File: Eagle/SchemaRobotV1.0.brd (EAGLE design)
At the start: 106 x 60 mm, 24 parts, among them J1 Connector US1, J2 Connector US 2, J3 Connector US 2, J4 Connector H-Brug, J5 Connector IR voeding, J6 Connector IR signalen, J7 Connector batterij 12v, J9 Connector HC-05

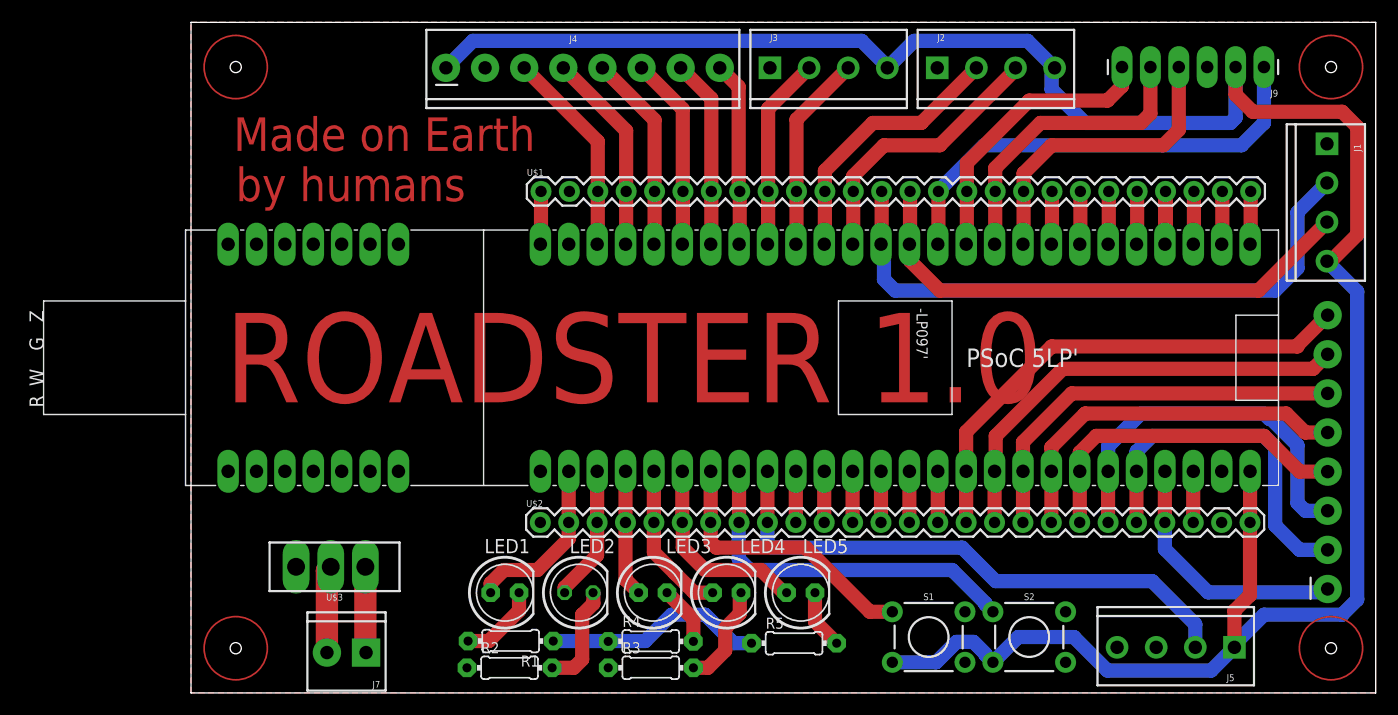
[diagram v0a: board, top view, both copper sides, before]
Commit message: eagle
meer padjes van top naar bottom
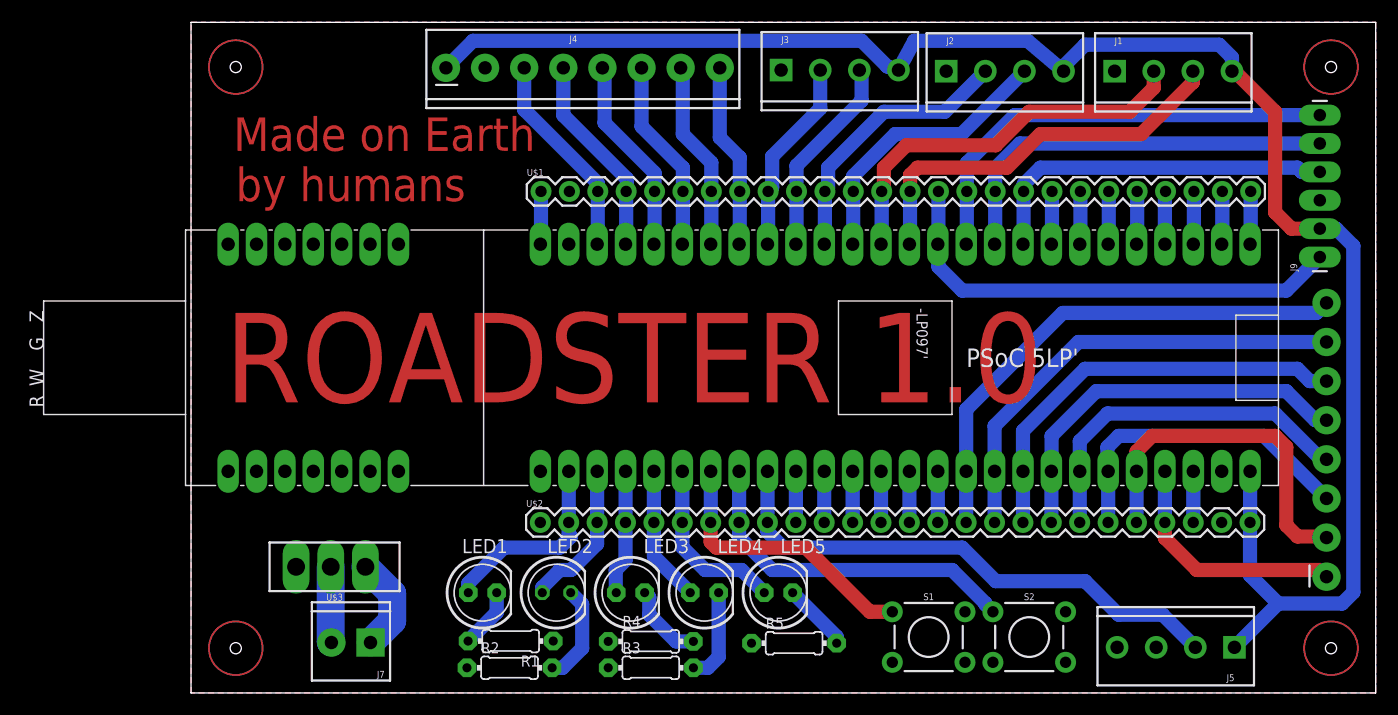
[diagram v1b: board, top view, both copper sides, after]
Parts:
- moved J1 20.1 mm to (82.6, 55.6), turned to 0 degrees
- moved J9 17.7 mm to (101.0, 39.0), turned to 90 degrees
- moved LED1 2.00 mm to (26.1, 8.97)
- moved LED2 2.00 mm to (32.7, 8.97)
- moved LED3 2.00 mm to (39.3, 8.97)
- moved LED4 2.00 mm to (45.9, 8.97)
- moved LED5 2.00 mm to (52.6, 8.97)
- moved J6 1.10 mm to (101.6, 10.4)
- moved J3 1.02 mm to (52.8, 55.7)
- moved J7 0.98 mm to (16.1, 4.51)
- moved J2 0.85 mm to (67.6, 55.6)
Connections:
- net GND: now also S1.3, S2.3
- net VCC: no longer S1.3, S2.3
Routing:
- net VCC: track 206.8 -> 157.0 mm
- net GND: track 19.8 -> 0.00 mm
- net P12.2: track 55.0 -> 35.5 mm
- net P12.5: track 25.7 -> 40.6 mm
- net P12.3: track 47.2 -> 35.9 mm
- net P12.6: track 26.9 -> 36.8 mm
- net P0.5: track 34.3 -> 29.1 mm
- net P12.7: track 27.5 -> 32.7 mm
- net P2.3: track 9.70 -> 4.75 mm
- net P3.0: track 15.5 -> 17.7 mm
- net P3.4: track 17.8 -> 15.8 mm
- net N$2: track 7.30 -> 5.39 mm
- net P0.2: track 36.3 -> 38.1 mm
- net P3.7: track 49.8 -> 48.0 mm
- net P3.3: track 14.0 -> 12.2 mm
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- added copper zone on layer 16, net GND

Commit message: eagle
padjes verbeterd
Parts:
- LED2: device led:LED5MM -> SchemaRobotV1.0:LED_LED5MM
- moved S1 2.00 mm to (64.0, 5.00)
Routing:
- net P3.5: track 25.2 -> 23.2 mm
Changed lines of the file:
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@@
 <setting verticaltext="up"/>
 </settings>
-<grid distance="1" unitdist="mm" unit="mm" style="lines" multiple="1" display="no" altdistance="0.1" altunitdist="mm" altunit="mm"/>
+<grid distance="0.1" unitdist="mm" unit="mm" style="lines" multiple="1" display="no" altdistance="0.1" altunitdist="mm" altunit="mm"/>
 <layers>
-<layer number="1" name="Top" color="4" fill="1" visible="yes" active="yes"/>
+<layer number="1" name="Top" color="4" fill="1" visible="no" active="yes"/>
 <layer number="2" name="Route2" color="1" fill="3" visible="no" active="no"/>
 <layer number="3" name="Route3" color="4" fill="3" visible="no" active="no"/>
@@
 <attribute name="VALUE" x="27.2804" y="6.1666" size="1.27" layer="27" ratio="10"/>
 </element>
-<element name="LED2" library="led" library_urn="urn:adsk.eagle:library:259" package="LED5MM" package3d_urn="urn:adsk.eagle:package:15799/2" value="3.3V" x="32.7" y="8.97" smashed="yes">
+<element name="LED2" library="SchemaRobotV1.0" package="LED_LED5MM" value="3.3V" x="32.7" y="8.97" smashed="yes">
 <attribute name="NAME" x="31.875" y="12.5034" size="1.27" layer="25" ratio="10"/>
 <attribute name="VALUE" x="32.9004" y="6.1666" size="1.27" layer="27" ratio="10"/>
@@
 <element name="U$2" library="SchemaRobotV1.0" package="SPARKFUN-CONNECTORS_1X26" value="SPARKFUN-CONNECTORS_CONN_26" x="31.254" y="15.254"/>
 <element name="J9" library="SchemaRobotV1.0" package="SPARKFUN-CONNECTORS_1X06_LONGPADS" value="Connector HC-05" x="101" y="39" rot="R90"/>
-<element name="S1" library="SchemaRobotV1.0" package="SPARKFUN-SWITCHES_TACTILE_SWITCH_PTH_6.0MM" value="SPARKFUN-SWITCHES_MOMENTARY-SWITCH-SPST-PTH-6.0MM" x="66" y="5">
-<attribute name="PROD_ID" value=" SWCH-08441" x="66" y="5" size="1.778" layer="27" display="off"/>
-<attribute name="SF_SKU" value="COM-00097" x="66" y="5" size="1.778" layer="27" display="off"/>
+<element name="S1" library="SchemaRobotV1.0" package="SPARKFUN-SWITCHES_TACTILE_SWITCH_PTH_6.0MM" value="SPARKFUN-SWITCHES_MOMENTARY-SWITCH-SPST-PTH-6.0MM" x="64" y="5">
+<attribute name="PROD_ID" value=" SWCH-08441" x="64" y="5" size="1.778" layer="27" display="off"/>
+<attribute name="SF_SKU" value="COM-00097" x="64" y="5" size="1.778" layer="27" display="off"/>
 </element>
 <element name="S2" library="SchemaRobotV1.0" package="SPARKFUN-SWITCHES_TACTILE_SWITCH_PTH_6.0MM" value="SPARKFUN-SWITCHES_MOMENTARY-SWITCH-SPST-PTH-6.0MM" x="75" y="5">
@@
 <contactref element="U$2" pad="26"/>
 <contactref element="J9" pad="2"/>
-<wire x1="78.07" y1="55.63" x2="74.851" y2="58.349" width="1.27" layer="16"/>
-<wire x1="64.719" y1="58.349" x2="63.3" y2="55.73" width="1.27" layer="16"/>
-<wire x1="74.851" y1="58.349" x2="64.719" y2="58.349" width="1.27" layer="16"/>
-<wire x1="22.81" y1="55.93" x2="25.229" y2="58.349" width="1.27" layer="16"/>
-<wire x1="25.229" y1="58.349" x2="60" y2="58.349" width="1.27" layer="16"/>
-<wire x1="60" y1="58.349" x2="62.3" y2="56.049" width="1.27" layer="16"/>
-<wire x1="62.3" y1="56.049" x2="63.3" y2="55.73" width="1.27" layer="16"/>
 <wire x1="101" y1="41.54" x2="98.46" y2="41.54" width="1.27" layer="1"/>
 <wire x1="97" y1="43" x2="97" y2="52" width="1.27" layer="1"/>
@@
 <wire x1="93.37" y1="55.63" x2="93.14" y2="55.63" width="1.27" layer="1"/>
 <wire x1="98.46" y1="41.54" x2="97" y2="43" width="1.27" layer="1"/>
-<wire x1="78.07" y1="55.63" x2="78.07" y2="56.07" width="1.27" layer="16"/>
-<wire x1="78.07" y1="56.07" x2="80" y2="58" width="1.27" layer="16"/>
-<wire x1="80" y1="58" x2="92" y2="58" width="1.27" layer="16"/>
-<wire x1="93.14" y1="56.86" x2="93.14" y2="55.63" width="1.27" layer="16"/>
-<wire x1="92" y1="58" x2="93.14" y2="56.86" width="1.27" layer="16"/>
 <wire x1="94.76" y1="19.83" x2="94.76" y2="15.26" width="1.27" layer="16"/>
 <wire x1="94.76" y1="15.26" x2="94.754" y2="15.254" width="1.27" layer="16"/>
@@
 <wire x1="94.754" y1="15.254" x2="94.754" y2="10.526" width="1.27" layer="16"/>
 <wire x1="94.754" y1="10.526" x2="97.28" y2="8" width="1.27" layer="16"/>
+<wire x1="25.229" y1="58.349" x2="22.81" y2="55.93" width="1.27" layer="16"/>
+<wire x1="63.3" y1="55.73" x2="60.681" y2="58.349" width="1.27" layer="16"/>
+<wire x1="60.681" y1="58.349" x2="25.229" y2="58.349" width="1.27" layer="16"/>
+<wire x1="63.3" y1="55.73" x2="65.919" y2="58.349" width="1.27" layer="16"/>
+<wire x1="65.919" y1="58.349" x2="76" y2="58.349" width="1.27" layer="16"/>
+<wire x1="76" y1="58.349" x2="78.07" y2="56.279" width="1.27" layer="16"/>
+<wire x1="78.07" y1="56.279" x2="78.07" y2="55.63" width="1.27" layer="16"/>
+<wire x1="78.07" y1="55.63" x2="80.789" y2="58.349" width="1.27" layer="16"/>
+<wire x1="93.14" y1="56.86" x2="93.14" y2="55.63" width="1.27" layer="16"/>
+<wire x1="80.789" y1="58.349" x2="91.651" y2="58.349" width="1.27" layer="16"/>
+<wire x1="91.651" y1="58.349" x2="93.14" y2="56.86" width="1.27" layer="16"/>
 </signal>
 <signal name="P1.7">
@@
 <wire x1="46.494" y1="15.254" x2="46.494" y2="13.506" width="1.27" layer="1"/>
 <wire x1="46.494" y1="13.506" x2="47" y2="13" width="1.27" layer="1"/>
-<wire x1="60.7394" y1="7.2606" x2="62.7488" y2="7.2606" width="1.27" layer="1"/>
+<wire x1="60.7394" y1="7.2606" x2="60.7488" y2="7.2606" width="1.27" layer="1"/>
 <wire x1="47" y1="13" x2="55" y2="13" width="1.27" layer="1"/>
 <wire x1="55" y1="13" x2="60.7394" y2="7.2606" width="1.27" layer="1"/>
@@
 </board>
 </drawing>
-<compatibility>
-<note version="8.2" severity="warning">
-Since Version 8.2, EAGLE supports online libraries. The ids
-of those online libraries will not be understood (or retained)
-with this version.
-</note>
-<note version="8.3" severity="warning">
-Since Version 8.3, EAGLE supports URNs for individual library
-assets (packages, symbols, and devices). The URNs of those assets
-will not be understood (or retained) with this version.
-</note>
-<note version="8.3" severity="warning">
-Since Version 8.3, EAGLE supports the association of 3D packages
-with devices in libraries, schematics, and board files. Those 3D
-packages will not be understood (or retained) with this version.
-</note>
-</compatibility>
 </eagle>
